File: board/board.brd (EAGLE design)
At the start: 185.4 x 44.5 mm, 91 parts, among them IC1 LM1117-3.3, IC2 4052SO16, IC3 RASPBERRY_PICOSMD, X1 DF51K-2X4, X10 MOLEX_MICROFIT3.0-2X3, X2 DF51K-2X4, X3 DF51K-2X4, X4 ATF13-2P, X5 DF51K-2X4, X6 ATF13-2P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

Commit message: Version 2.1 board with corrected Pi Power MOSFET and Temperature Connections
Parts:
- moved R38 2.54 mm to (166.4, 31.8)
- moved R39 2.54 mm to (168.9, 31.8)
- moved R40 2.54 mm to (171.4, 31.8)
- moved R41 2.54 mm to (174.0, 31.8)
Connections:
- removed net N$26: IC2.14, R40.1, X9.P$3
- removed net N$34: IC2.12, R39.1, X9.P$5
- removed net N$68: IC2.15, R41.1, X9.P$1
- new net N$63: IC2.11, R39.1, X9.P$5
- new net N$70: IC2.15, R40.1, X9.P$3
- new net N$71: IC2.12, R41.1, X9.P$1
- net DEBUG_LED: now also IC3.P$27; no longer IC3.P$21
- net N$35: now also IC2.14; no longer IC2.11
- net PAS_SEAT_EN: now also IC3.P$21; no longer IC3.P$22
- net PAS_SEAT_LED1: now also IC3.P$25; no longer IC3.P$26
- net PAS_SEAT_LED2: now also IC3.P$24; no longer IC3.P$25
- net PAS_SEAT_LED3: now also IC3.P$22; no longer IC3.P$24
- net PAS_SEAT_SW: now also IC3.P$26; no longer IC3.P$27
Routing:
- net N$35: track 7.94 -> 27.6 mm
- net DEBUG_LED: track 56.6 -> 70.3 mm, vias 3 -> 1
- net N$71: track 0.00 -> 13.0 mm
- net N$70: track 0.00 -> 10.7 mm, vias 0 -> 1
- net N$63: track 0.00 -> 10.2 mm
- net N$26: track 7.64 -> 0.00 mm
- net N$68: track 7.56 -> 0.00 mm
- net N$34: track 7.41 -> 0.00 mm
- net PAS_SEAT_LED3: track 58.9 -> 52.5 mm
- net PAS_SEAT_EN: track 46.2 -> 41.9 mm
- net PAS_SEAT_LED1: track 79.2 -> 75.4 mm
- net PAS_SEAT_SW: track 96.6 -> 92.8 mm
- net PAS_SEAT_LED2: track 69.0 -> 65.2 mm
- net N$16: track 6.25 -> 9.41 mm
- net N$15: track 4.98 -> 7.77 mm
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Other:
- board text added: "HEATER_CONTROL_v2.1"

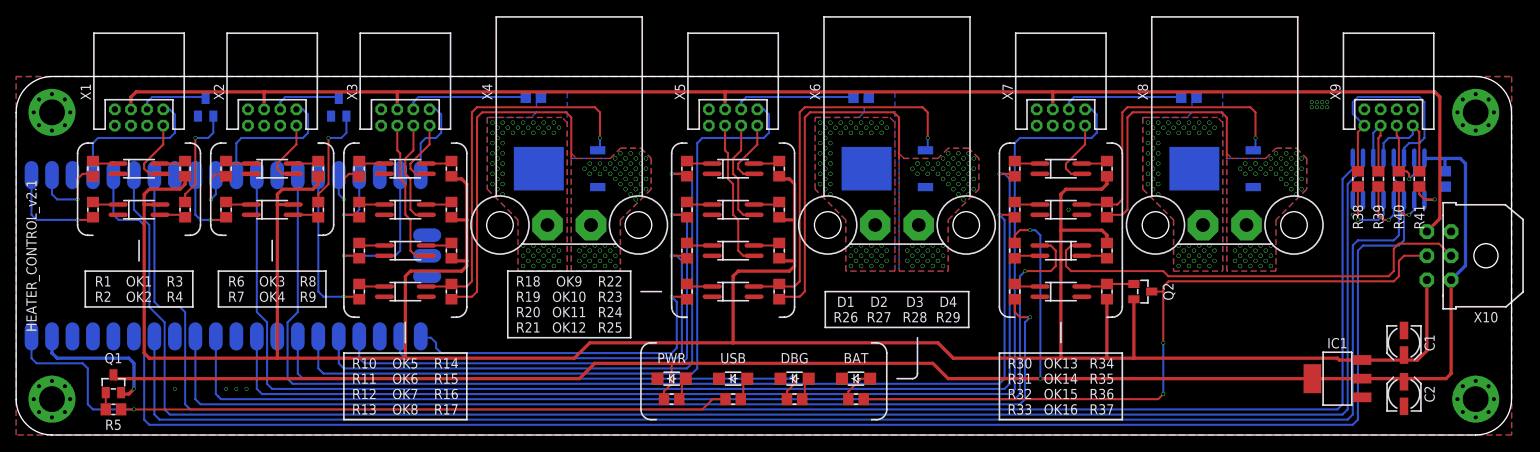
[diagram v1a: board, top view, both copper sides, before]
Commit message: Updated board layout with pulldown resistors for N channel MOSFETS
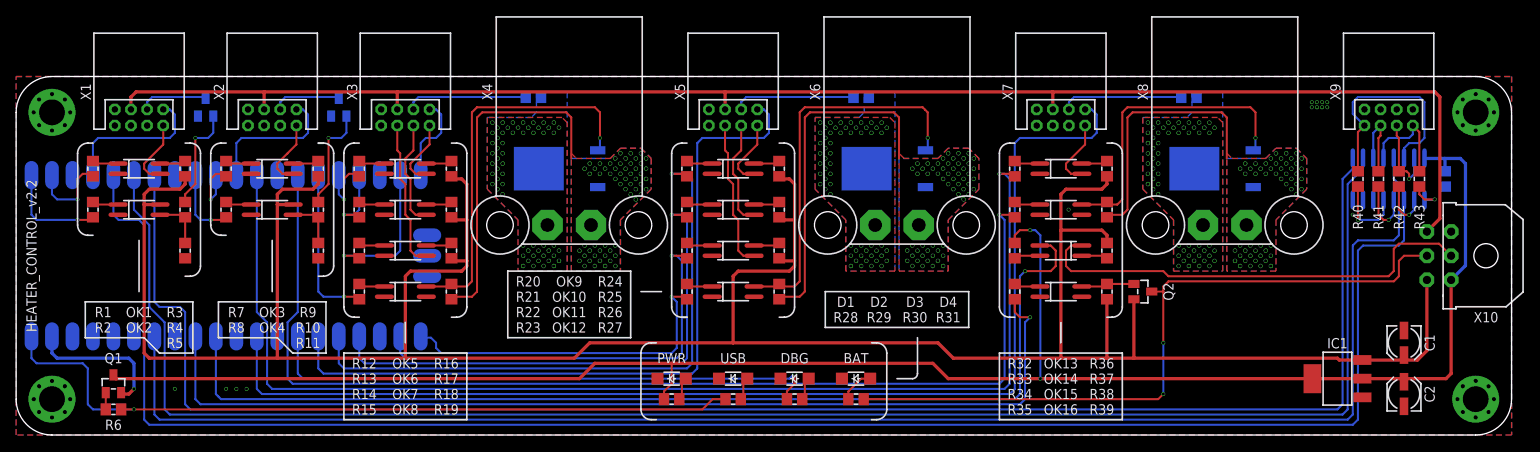
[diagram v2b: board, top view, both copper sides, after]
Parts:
- added R45, R46: 560, SMD:R0805
- R10, R19, R6: value 120 -> 1k
- R11: value 120 -> 10k
- R14, R15, R22, R23, R8: value 560 -> 120
- R17, R25, R9: value 1k -> 560
- R18: value 120 -> 560
- R26: value (none) -> 560
- R27: value (none) -> 1k
- R30, R31: value 120 -> (none)
- R32, R35: value 1k -> 120
- R34: value 560 -> 1k
- R38: value 10k -> 560
- R39: value 10k -> 1k
- R42, R43: value 560 -> 10k
- R5: value 1k -> 10k
- moved R44 81.3 mm to (145.4, 41.9)
- moved R43 70.0 mm to (174.0, 31.8), flipped to the top, turned to 270 degrees
- moved R30 39.5 mm to (96.5, 4.45), turned to 180 degrees
- moved R39 36.4 mm to (135.3, 17.8)
- moved R6 33.0 mm to (12.1, 3.17), turned to 180 degrees
- moved R38 32.4 mm to (135.3, 22.9)
- moved R18 30.9 mm to (54.0, 22.9), turned to 270 degrees
- moved R19 30.9 mm to (54.0, 17.8)
- moved R31 30.7 mm to (104.1, 4.45), turned to 0 degrees
- moved R42 27.9 mm to (171.4, 31.8), flipped to the top, turned to 270 degrees
- moved R26 22.7 mm to (94.6, 22.9), turned to 270 degrees
- moved R5 21.6 mm to (21.0, 22.9), turned to 90 degrees
- moved R14 15.3 mm to (42.5, 22.9), turned to 90 degrees
- moved R15 15.3 mm to (42.5, 17.8)
- moved R22 15.3 mm to (83.2, 22.9), turned to 90 degrees
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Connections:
- net +12V: now also R17.2, R18.2, R25.2, R26.2, R36.2, R38.1, R39.2, R9.2; no longer R14.2, R15.2, R22.2, R23.2, R34.2, R36.1, R37.2, R8.2
- net +3V3: now also R28.2, R34.2; no longer R26.2, R32.2
- net BATTERY_CHARGE: now also R35.1; no longer R33.1
- net DEBUG_LED: now also R30.2; no longer R28.2
- net DRV_SEAT_EN: now also R15.2; no longer R13.2
- net DRV_SEAT_LED1: now also R12.1; no longer R10.1
- net DRV_SEAT_LED2: now also R13.1; no longer R11.1
- net DRV_SEAT_LED3: now also R14.1; no longer R12.1
- net ENGINE_RUN_OUT: now also R31.2; no longer R29.2
- net GND: now also R11.1, R5.1
- net MIRROR_EN: now also R8.2; no longer R7.2
- net MIRROR_LED1: now also R7.1; no longer R6.1
- net N$10: now also R24.1; no longer R22.1
- net N$11: now also R25.1; no longer R23.1
- net N$12: now also R26.1; no longer R24.1
- net N$15: now also R41.2; no longer R39.2
- net N$16: now also R40.2; no longer R38.2
- net N$24: now also R7.2; no longer R6.2
- net N$25: now also R32.2; no longer R30.2
- net N$27: now also R28.1; no longer R26.1
- net N$28: now also R12.2; no longer R10.2
- net N$29: now also R13.2; no longer R11.2
- net N$3: now also R9.1; no longer R8.1
- net N$30: now also R14.2; no longer R12.2
- net N$31: now also R20.2; no longer R18.2
- net N$32: now also R21.2; no longer R19.2
- net N$33: now also R22.2; no longer R20.2
- net N$35: now also R40.1; no longer R38.1
- net N$37: now also R5.2
- net N$4: now also R36.1; no longer R34.1
- net N$41: now also R10.2, R11.2; no longer R9.2
- net N$42: now also R8.1; no longer R7.1
- net N$43: now also R10.1; no longer R9.1
- net N$44: now also R33.1; no longer R31.1
- net N$45: now also R37.1; no longer R35.1
- net N$46: now also R37.2; no longer R35.2
- net N$47: now also R44.2; no longer R42.2
- net N$48: now also R44.1; no longer R42.1
- net N$49: now also R46.1; no longer R44.1
- net N$5: now also R43.2; no longer R41.2
- net N$50: now also R46.2; no longer R44.2
- net N$51: now also R15.1; no longer R13.1
- net N$52: now also R19.1; no longer R17.1
- net N$53: now also R19.2; no longer R17.2
- net N$54: now also R45.1; no longer R43.1
- net N$55: now also R45.2; no longer R43.2
- net N$56: now also R38.2; no longer R36.2
- net N$57: now also R27.1; no longer R25.1
- net N$58: now also R23.1; no longer R21.1
- net N$59: now also R27.2; no longer R25.2
- net N$6: now also R42.2; no longer R40.2
- net N$60: now also R34.1; no longer R32.1
- net N$61: now also R35.2; no longer R33.2
- net N$62: now also R39.1; no longer R37.1
- net N$63: now also R41.1; no longer R39.1
- net N$64: now also R6.2; no longer R5.2
- net N$66: now also R29.1; no longer R27.1
- net N$67: now also R31.1; no longer R29.1
- net N$69: now also R30.1; no longer R28.1
- net N$7: now also R16.1; no longer R14.1
- net N$70: now also R42.1; no longer R40.1
- net N$71: now also R43.1; no longer R41.1
- net N$8: now also R17.1; no longer R15.1
- net N$9: now also R18.1; no longer R16.1
- net PAS_SEAT_EN: now also R23.2; no longer R21.2
- net PAS_SEAT_LED1: now also R20.1; no longer R18.1
- net PAS_SEAT_LED2: now also R21.1; no longer R19.1
- net PAS_SEAT_LED3: now also R22.1; no longer R20.1
- net USB_POWER: now also R29.2, R6.1; no longer R27.2, R5.1
- net WHEEL_EN: now also R33.2; no longer R31.2
- net WHEEL_LED1: now also R32.1; no longer R30.1
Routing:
- net N$41: track 3.25 -> 6.43 mm
- net N$37: track 3.25 -> 6.43 mm
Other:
- board text added: "HEATER_CONTROL_v2.2"
- board text removed: "HEATER_CONTROL_v2.1"
